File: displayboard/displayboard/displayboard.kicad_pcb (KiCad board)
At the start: 2 copper layers, 105.3 x 56.3 mm, 8 parts

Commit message: V1.2
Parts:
- removed the REF** at (169.7, 68.8)
- added ?: , , F.Cu at (213.9, 27.2)
- added ?: , , F.Cu at (275.1, 27.2)
- added ?: , , F.Cu at (275.1, 141.6)
- added C1: C_Small, Capacitor_SMD:C_0805_2012Metric, B.Cu at (255.9, 35.3)
- added C2: C_Small, Capacitor_SMD:C_0805_2012Metric, B.Cu at (256.6, 39.5)
- added SW1: RotaryEncoder_Switch, Rotary_Encoder:RotaryEncoder_Alps_EC11E-Switch_Vertical_H20mm, F.Cu at (259.7, 36.1)
- moved REF** 192.5 mm to (273.0, 121.3), turned to 90 degrees
- moved REF** 167.1 mm to (230.0, 121.3), turned to 90 degrees
- moved REF** 125.7 mm to (273.0, 55.9), turned to 90 degrees
- moved REF** 117.9 mm to (229.8, 84.7), turned to 0 degrees
- moved REF** 81.7 mm to (230.0, 55.9), turned to 90 degrees
- moved REF** 79.9 mm to (242.7, 42.5), turned to 180 degrees
- moved REF** 67.4 mm to (230.8, 42.4), turned to 90 degrees
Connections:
- REF** pad 1: GND -> Net-(A1-GPIO20)
- REF** pad 2: PICO_3V3 -> Net-(A1-GPIO21)
- REF** pad 3: Net-(A1-GPIO21) -> GND
- REF** pad 4: Net-(A1-GPIO20) -> PICO_3V3
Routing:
- net AGND: track 57.3 -> 71.1 mm, vias 0 -> 1
- net Net-(A1-GPIO20): track 61.5 -> 54.5 mm, vias 0 -> 2
- net PICO_3V3: track 52.8 -> 57.0 mm
- net Net-(A1-GPIO21): track 56.0 -> 55.0 mm
- net ADC0_GP27: track 17.4 -> 18.0 mm, vias 0 -> 1
- net GND: vias 0 -> 1
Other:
- board size 105.3 x 56.3 mm -> 71.8 x 124.6 mm

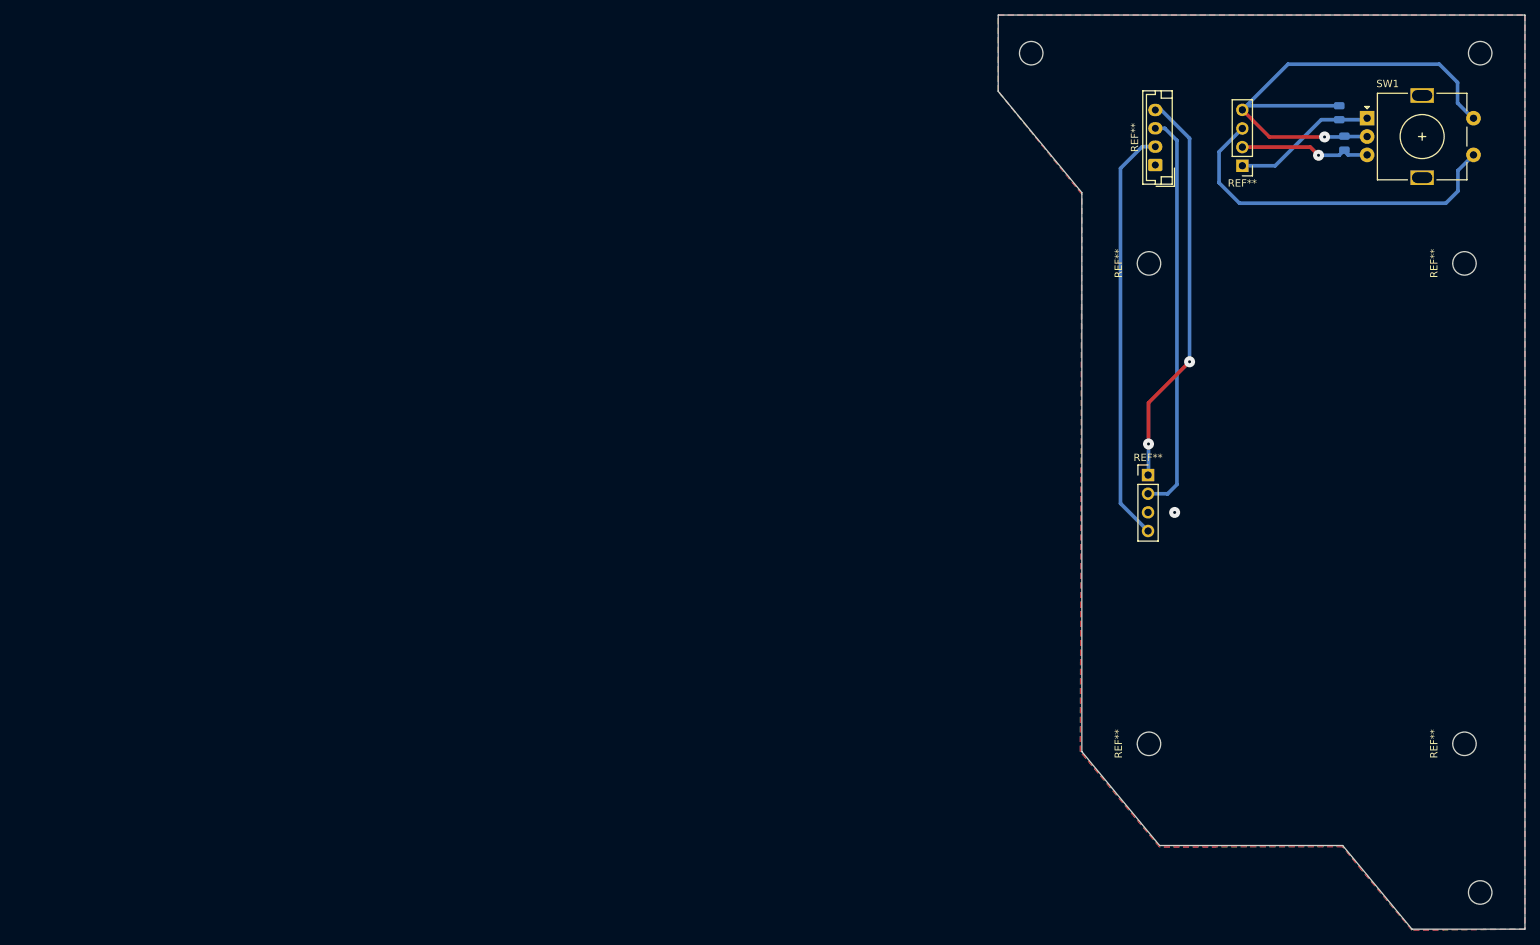
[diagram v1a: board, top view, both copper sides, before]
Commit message: Ready boards
powerboard, displayboard and mainboard all ready to mill
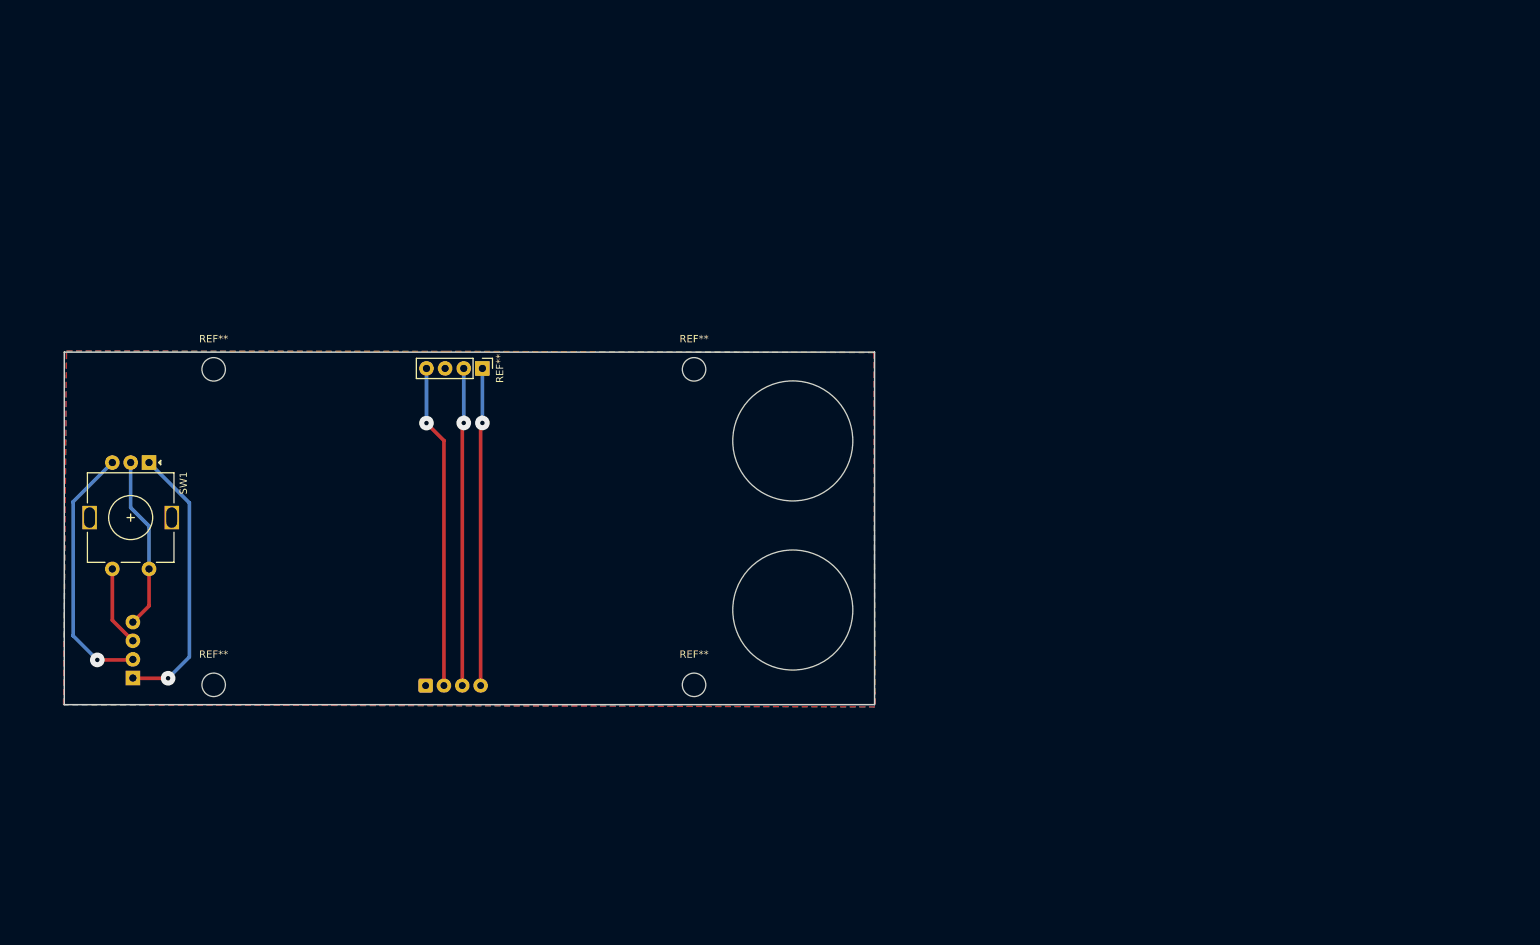
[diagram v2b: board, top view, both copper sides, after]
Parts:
- removed the ? at (213.9, 27.2)
- removed the ? at (275.1, 27.2)
- removed C1, C2: C_Small, Capacitor_SMD:C_0805_2012Metric
- added ?: , , F.Cu at (181.4, 80.0)
- REF** (x2): moved to B.Cu
- moved SW1 172.5 mm to (93.7, 83.0), turned to -90 degrees
- moved REF** 170.7 mm to (102.5, 113.3), turned to 0 degrees
- moved REF** 166.6 mm to (91.5, 112.4), turned to 0 degrees
- moved REF** 137.3 mm to (102.5, 70.3), turned to 0 degrees
- moved REF** 122.2 mm to (131.3, 113.4), turned to 0 degrees
- moved REF** 119.7 mm to (167.9, 113.3), turned to 0 degrees
- moved ? 101.3 mm to (181.4, 103.1), turned to -90 degrees
- moved REF** 91.9 mm to (139.1, 70.2), turned to -90 degrees
- moved REF** 63.7 mm to (167.9, 70.3), turned to 0 degrees
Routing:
- net AGND: track 71.1 -> 23.7 mm, vias 1 -> 0
- net ADC0_GP28: track 48.9 -> 10.9 mm
- net ADC0_GP26: track 19.7 -> 37.7 mm, vias 0 -> 1
- net ADC0_GP27: track 18.0 -> 35.4 mm
- net PICO_3V3: track 57.0 -> 44.2 mm, vias 0 -> 1
- net Net-(A1-GPIO21): track 55.0 -> 43.6 mm, vias 0 -> 1
- net Net-(A1-GPIO20): track 54.5 -> 43.7 mm, vias 2 -> 1
- net GND: vias 1 -> 0
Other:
- board size 71.8 x 124.6 mm -> 110.5 x 48 mm
